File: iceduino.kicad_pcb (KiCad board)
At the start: 4 copper layers, 80 x 100 mm, 245 parts, among them J1 7-17 V IN, J2 USB_B_Micro, J3 Conn_01x08, J4 Conn_01x06, J5 Conn_01x10, J6 Conn_01x08, Q1 DMP3099L-7, Q2 Q_NMOS_GSD, Q3 Q_NMOS_GSD, Q4 Q_NMOS_GSD, SW1 SW_Push, SW2 SW_Push, SW3 SW_Push, SW4 SW_Push, SW5 SW_Push, SW6 JS202011SCQN, SW7 JS202011SCQN, SW8 SW_Push, SW9 JS202011SCQN, U1 ICE40HX4K-TQ144, U10 MAX40200AUK, U11 MAX40200AUK, U12 TXS0108EPW, U13 MAX11614, U14 TXS0108EPW, U15 93LCxxBT-I_OT, U16 FT2232H, U17 SN74LVC1G32DBVR, U18 SN74LVC2T45DCUR, U19 SN74LVC2T45DCUR, U2 MAX40200AUK, U20 SN74AXC4T245PWR, U21 SN74LVC2T45DCUR, U22 SN74LVC2T45DCUR, U23 SN74LVC2G07DCKR, U24 W25Q64JV, U3 TPS562201, U4 MAX40200AUK, U5 MAX40200AUK, U6 TLV62568APDRLR, U7 TLV62568APDRLR, U8 IS61WV5128EDBLL-10TLI, U9 MIC5365-3.3YC5, Y1 ECS-3225S33-500-FN-TR, Y2 ECS-3225S33-120-FN-TR

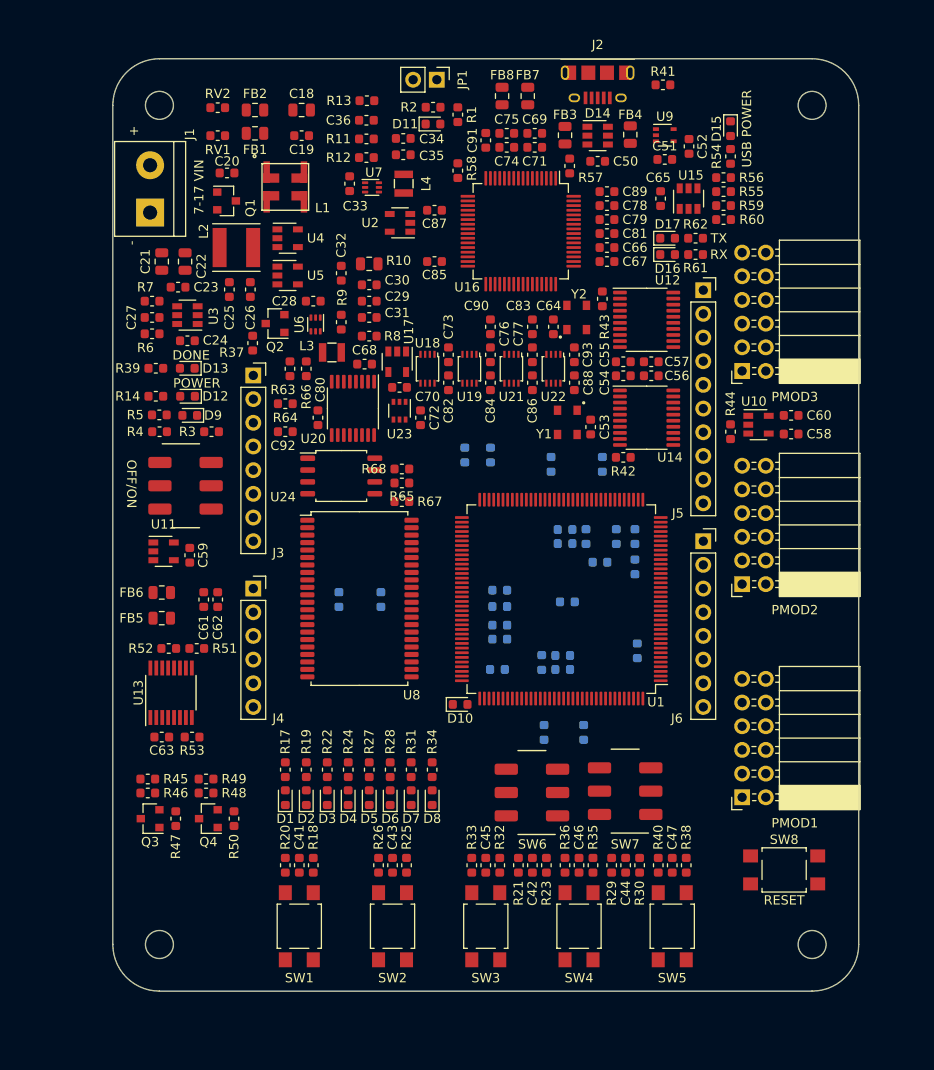
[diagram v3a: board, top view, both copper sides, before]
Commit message: FPGA PINs for PMOD reorganized FPGA PINs for Arduino Header reorganized Trace routing partially ready
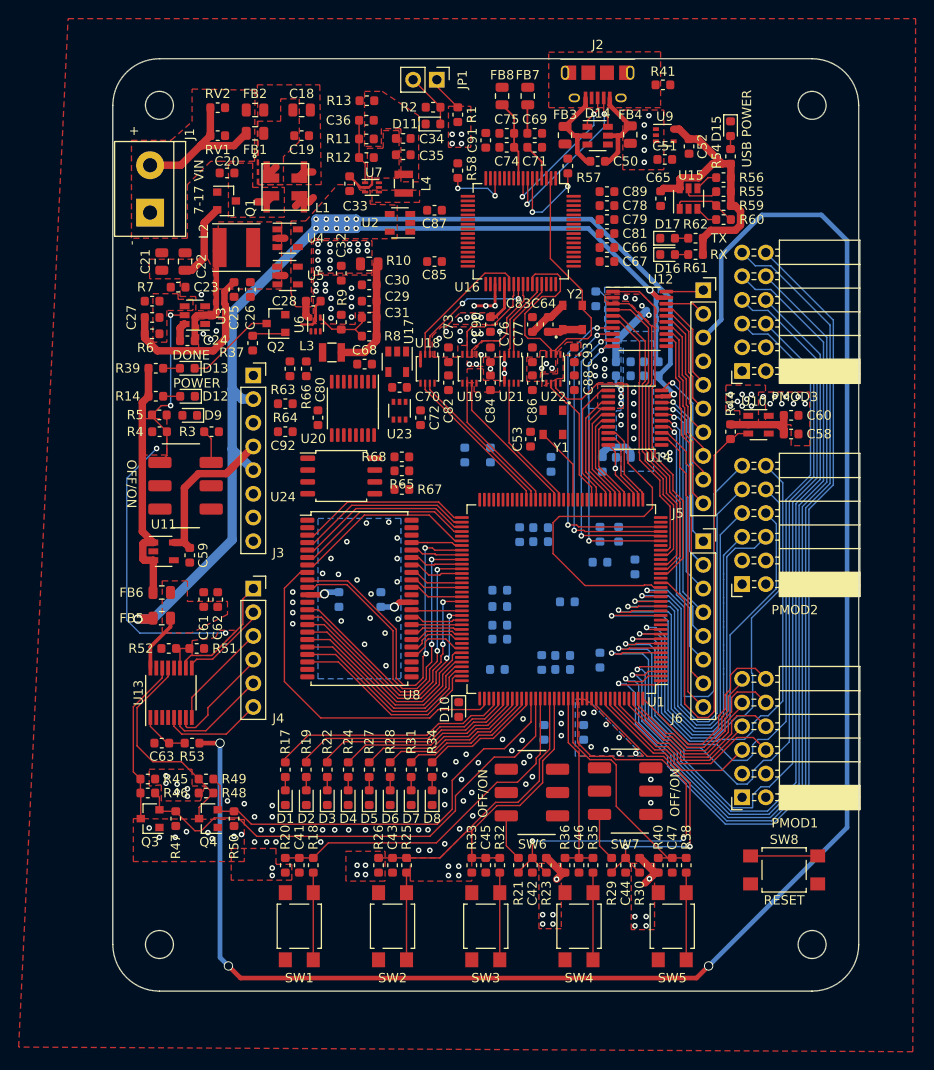
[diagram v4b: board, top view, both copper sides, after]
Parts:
- C54, C55, C56, C57, R42, R43: moved to B.Cu
- moved R15 7.12 mm to (83.6, 91.0)
- moved C53 6.58 mm to (84.8, 80.8)
- moved C4 4.12 mm to (92.2, 104.5)
- moved C37 2.63 mm to (85.9, 90.3)
- moved C38 2.63 mm to (85.9, 91.8)
- moved C17 1.77 mm to (92.2, 91.0)
- moved C3 1.77 mm to (94.2, 91.0)
- moved Y1 1.55 mm to (87.2, 79.0)
- moved R65 1.30 mm to (71.0, 84.2)
- moved R67 1.30 mm to (71.0, 86.2)
- moved R68 1.30 mm to (71.0, 82.7)
- moved U14 1.25 mm to (96.0, 78.5)
- moved U3 0.80 mm to (48.8, 67.5)
- moved U12 0.76 mm to (96.5, 67.9)
- moved R43 0.70 mm to (91.8, 65.8), turned to 270 degrees
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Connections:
- U1 pad 1: /P9_3 -> /P7_3
- U1 pad 10: /P9_2 -> /P4_3
- U1 pad 11: /P2_3 -> /P7_2
- U1 pad 12: /P10_2 -> /P8_2
- U1 pad 15: /P4_2 -> /P9_2
- U1 pad 16: /P1_3 -> /P10_2
- U1 pad 17: /P3_2 -> /P4_2
- U1 pad 18: /P7_2 -> /P3_2
- U1 pad 2: /P10_3 -> /P1_3
- U1 pad 24: /FPGA_INO_SCK -> /FPGA_INO_SCL
- U1 pad 25: /FPGA_INO_MISO -> /FPGA_INO_SDA
- U1 pad 26: /FPGA_INO_SDA -> /FPGA_INO_SCK
- U1 pad 28: /FPGA_INO_SCL -> /FPGA_INO_MISO
- U1 pad 3: /P4_3 -> /P8_3
- U1 pad 31: /FPGA_INO_SS -> /OE1
- U1 pad 32: /FPGA_INO_D9 -> /FPGA_INO_D8
- U1 pad 33: /FPGA_INO_D8 -> /FPGA_INO_D9
- U1 pad 34: /OE1 -> /FPGA_INO_SS
- U1 pad 4: /P3_3 -> /P2_3
- U1 pad 7: /P8_3 -> /P9_3
- U1 pad 8: /P8_2 -> /P3_3
- U1 pad 9: /P7_3 -> /P10_3
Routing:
- net /HEADER/INO_AREF: track 0.00 -> 189.1 mm, vias 0 -> 3
- net +5V: track 0.00 -> 165.5 mm, vias 0 -> 13
- net /P1_3: track 0.00 -> 97.5 mm, vias 0 -> 1
- net /P7_3: track 0.00 -> 97.1 mm, vias 0 -> 1
- net /P9_3: track 0.00 -> 93.0 mm, vias 0 -> 1
- net /P3_3: track 0.00 -> 92.8 mm, vias 0 -> 1
- net /P2_3: track 0.00 -> 91.5 mm, vias 0 -> 1
- net /P8_3: track 0.00 -> 90.8 mm, vias 0 -> 1
- net /P10_3: track 0.00 -> 82.2 mm, vias 0 -> 1
- net /P4_3: track 0.00 -> 79.4 mm, vias 0 -> 1
- net /P7_2: track 0.00 -> 55.4 mm, vias 0 -> 1
- net /P9_2: track 0.00 -> 54.2 mm, vias 0 -> 1
- net /ADC_SDA_3V3: track 0.00 -> 54.1 mm
- net +3V3: track 0.00 -> 52.4 mm, vias 0 -> 58
- net /CLK_12M: track 0.00 -> 51.4 mm
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- added copper zone on F.Cu, net +1V2
- added copper zone on B.Cu, net +3V3
- added copper zone on F.Cu, net +3V3
- added copper zone on F.Cu, net +3V3_FTDI
- added copper zone on F.Cu, net +5V
- added copper zone on F.Cu, net /HEADER/ADC_VCC
- added copper zone on F.Cu, net /HEADER/PMOD_3V3
- added copper zone on In2.Cu, net /HEADER/PMOD_3V3
- added copper zone on F.Cu, net /Power/7-17VIN-5V_REGULATOR/5V_IN
- added copper zone on F.Cu, net /Power/7-17VIN-5V_REGULATOR/FB_5V
- added copper zone on F.Cu, net /Power/7-17VIN_PROTECTION/GND_IN
- added copper zone on F.Cu, net /Power/7-17VIN_PROTECTION/GND_IN_FILTERED
- added copper zone on F.Cu, net /Power/7-17VIN_PROTECTION/V_IN_CHOKE
- added copper zone on F.Cu, net /Power/7-17VIN_PROTECTION/V_IN_FILTERED
- added copper zone on F.Cu, net /USB_PROGRAMMER/1V8
- added copper zone on F.Cu, net /V_IN_PROTECTED
- added copper zone on B.Cu, net GND
- added copper zone on F.Cu, net GND
- added copper zone on In1.Cu, net GND
- added copper zone on F.Cu, net Net-(J2-Pad6)
- added copper zone on F.Cu, net Net-(L4-Pad1)
- added copper zone on F.Cu, net VBUS
- added copper zone on In2.Cu, net VBUS
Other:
- net class 17V2A added: clearance 0.2, trace_width 0.8, via_dia 0.8, via_drill 0.4
- net class Default: via_dia 0.8 -> 0.6; via_drill 0.4 -> 0.3
- rule via_min_size: 0.4 -> 0.6

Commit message: Board design completed Revision 1
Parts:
- C83: moved to B.Cu
- moved C83 8.02 mm to (84.5, 60.5), turned to 90 degrees
- moved C68 5.57 mm to (62.0, 75.2), turned to 90 degrees
- moved C37 2.06 mm to (83.9, 90.8)
- moved C38 2.06 mm to (83.9, 92.3)
- moved R15 2.06 mm to (81.6, 91.5)
- moved Y1 1.93 mm to (86.5, 80.8)
- moved R66 1.45 mm to (59.3, 73.2)
- moved C12 1.30 mm to (94.7, 94.5)
- moved R63 1.30 mm to (57.7, 73.2)
- moved C53 1.27 mm to (83.9, 79.9)
- moved R64 1.10 mm to (58.5, 78.1)
- moved C9 1.00 mm to (87.0, 84.5)
- moved C92 1.00 mm to (58.5, 81.0)
- moved C87 0.90 mm to (75.2, 55.8)
- moved C1 0.82 mm to (92.9, 94.5), turned to 270 degrees
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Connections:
- U1 pad 136: /P4_1 -> /P1_1
- U1 pad 137: /P10_1 -> /P7_1
- U1 pad 138: /P3_1 -> /P8_1
- U1 pad 141: /P2_1 -> /P10_1
- U1 pad 142: /P8_1 -> /P4_1
- U1 pad 143: /P1_1 -> /P3_1
- U1 pad 144: /P7_1 -> /P2_1
- U1 pad 26: /FPGA_INO_SCK -> /FPGA_INO_MISO
- U1 pad 28: /FPGA_INO_MISO -> /FPGA_INO_SCK
- U1 pad 37: /FPGA_INO_TX -> /FPGA_INO_RX
- U1 pad 38: /FPGA_INO_RX -> /FPGA_INO_TX
- U12 pad 16: /HEADER/INO_MISO -> /HEADER/INO_SCK
- U12 pad 17: /HEADER/INO_SCK -> /HEADER/INO_MISO
- U12 pad 4: /FPGA_INO_SCK -> /FPGA_INO_MISO
- U12 pad 5: /FPGA_INO_MISO -> /FPGA_INO_SCK
- U14 pad 12: /HEADER/INO_RX -> /HEADER/INO_TX
- U14 pad 13: /HEADER/INO_TX -> /HEADER/INO_RX
- U14 pad 8: /FPGA_INO_TX -> /FPGA_INO_RX
- U14 pad 9: /FPGA_INO_RX -> /FPGA_INO_TX
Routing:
- net /CRESET_B: track 7.20 -> 301.7 mm, vias 0 -> 9
- net +3V3: track 52.4 -> 134.9 mm, vias 58 -> 87
- net /Power/EN_LOW_VOLTAGE: track 3.61 -> 75.1 mm, vias 0 -> 5
- net +1V2: track 0.00 -> 62.3 mm, vias 14 -> 10
- net /USB_PROGRAMMER/1V8: track 4.47 -> 64.0 mm, vias 4 -> 6
- net /CDONE: track 3.65 -> 61.6 mm, vias 0 -> 6
- net /SCK: track 0.00 -> 36.2 mm, vias 0 -> 2
- net /SS: track 0.00 -> 36.0 mm, vias 0 -> 2
- net +3V3_FTDI: track 33.5 -> 66.8 mm, vias 7 -> 44
- net /USB_PROGRAMMER/FTDI_MISO: track 0.00 -> 32.0 mm, vias 0 -> 2
- net /P1_1: track 18.7 -> 49.9 mm
- net /USB_PROGRAMMER/FTDI_SCK: track 0.00 -> 30.4 mm
- net /FLASH_IO1: track 0.00 -> 29.5 mm
- net Net-(R63-Pad1): track 0.00 -> 27.5 mm, vias 0 -> 2
- net /USB_PROGRAMMER/FTDI_CDONE: track 0.00 -> 27.1 mm, vias 0 -> 2
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- added copper zone on B.Cu, net +1V2
- added copper zone on In2.Cu, net +3V3
- added copper zone on In2.Cu, net +3V3_FTDI
- added copper zone on In2.Cu, net /HEADER/ADC_VCC
- added copper zone on B.Cu, net /USB_PROGRAMMER/1V8
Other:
- rule trace_min: 0.15 -> 0
- board text added: "1"
- board text added: "2"
- board text added: "3"
- board text added: "4"
- board text added: "BOT"
- board text added: "TOP"

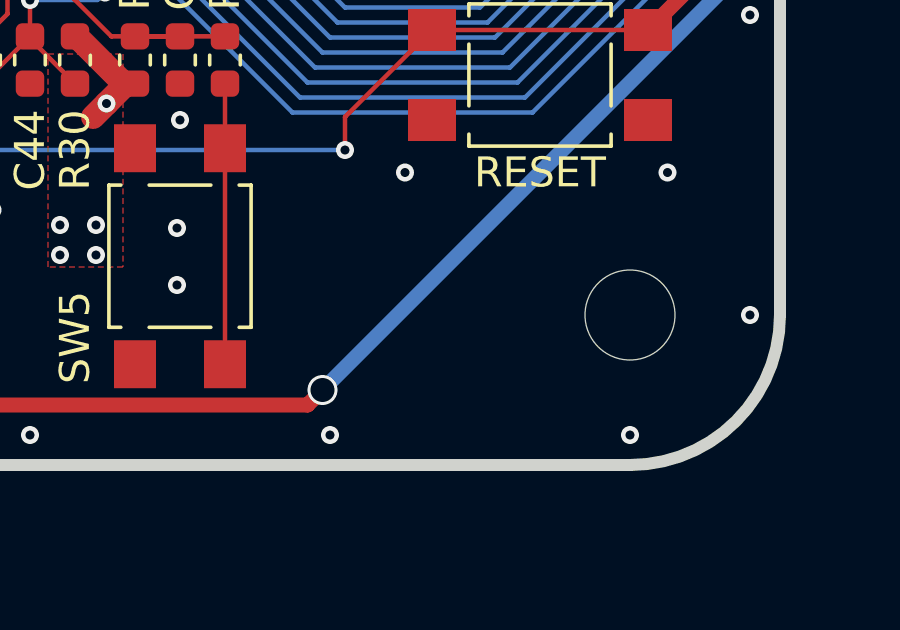
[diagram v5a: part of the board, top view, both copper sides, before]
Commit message: Added project description in kicad schematic sheets Added project name and OSHW logo on the board
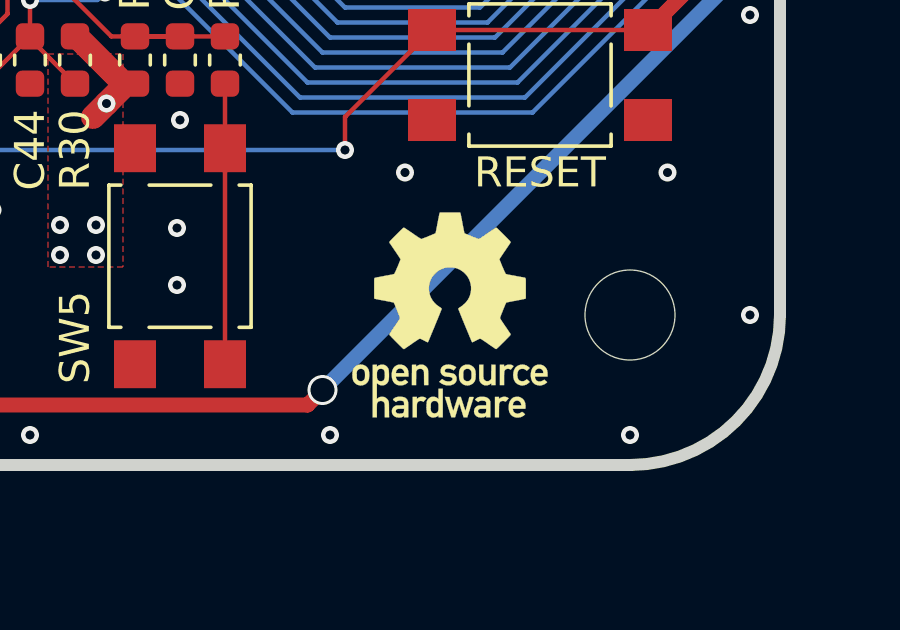
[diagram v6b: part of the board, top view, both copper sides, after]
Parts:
- added G***: LOGO, footprints:OSHW, B.Cu at (55.0, 46.0)
- added G***: LOGO, footprints:OSHW, F.Cu at (109.0, 135.0)
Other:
- board text added: "ICE40HX4K ICEduino educational breakout board 20200619_rev1"

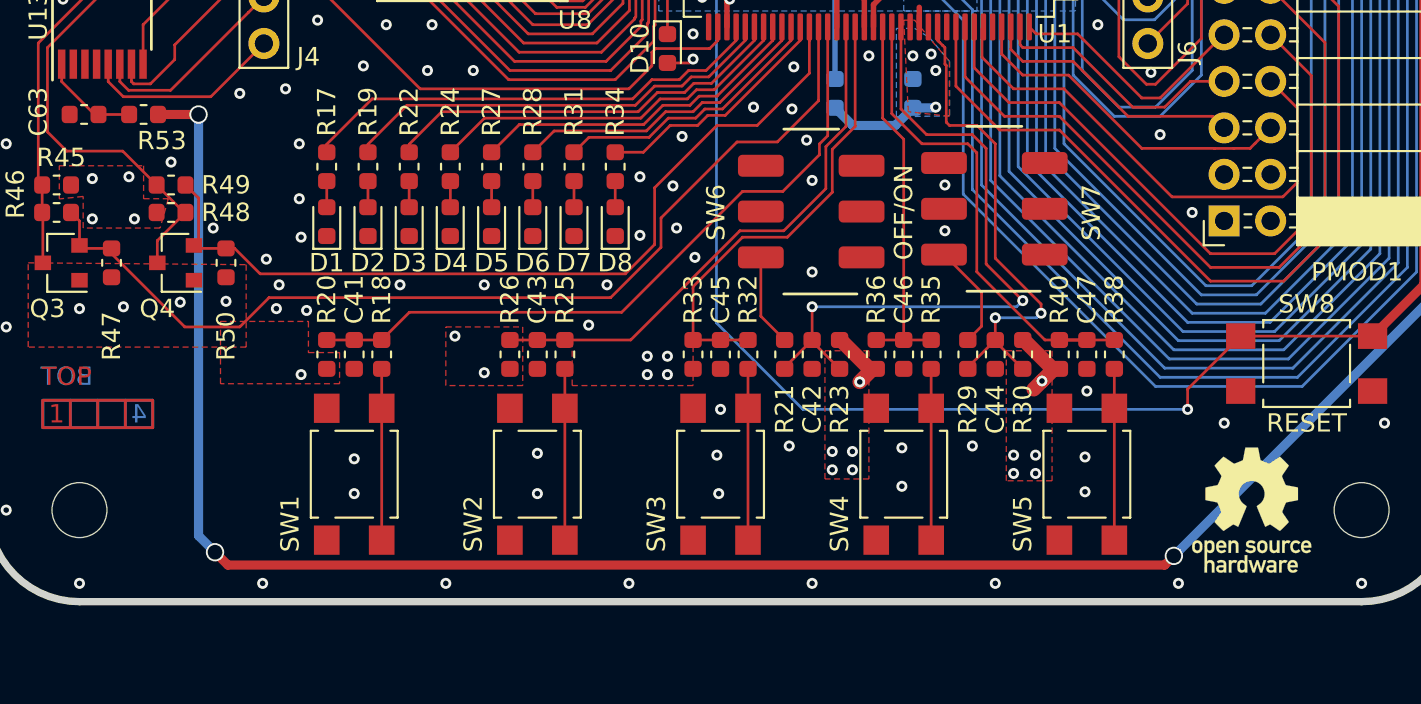
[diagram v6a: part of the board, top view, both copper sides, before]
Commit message: Bigger OSHW logo
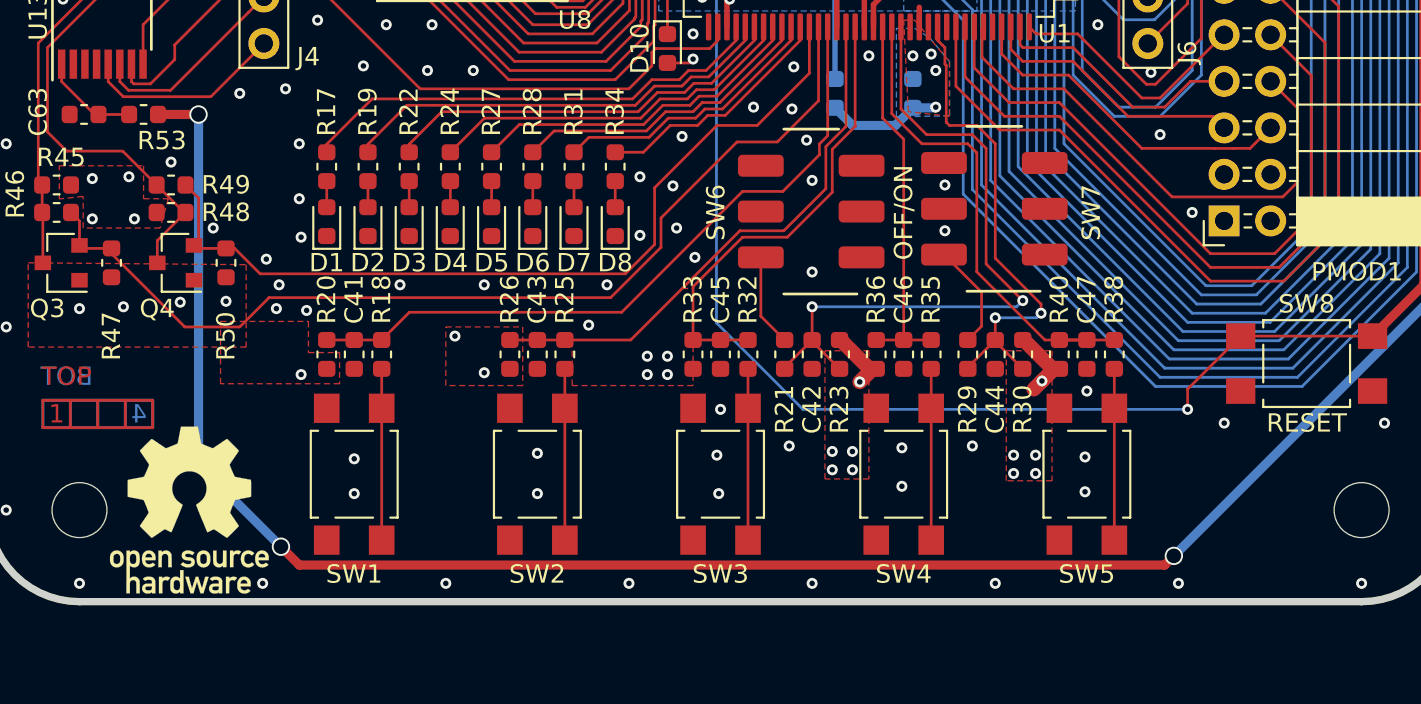
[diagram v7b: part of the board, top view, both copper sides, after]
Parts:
- removed the G*** at (55.0, 46.0)
- removed the G*** at (109.0, 135.0)
- added G***: LOGO, footprints:OSHW, B.Cu at (56.0, 47.0)
- added G***: LOGO, footprints:OSHW, F.Cu at (51.0, 135.0)
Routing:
- net /HEADER/INO_AREF: track 188.6 -> 186.4 mm

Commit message: Power layer was not entirely used
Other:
- rule trace_min: 0 -> 0.15
